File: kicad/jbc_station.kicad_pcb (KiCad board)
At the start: 2 copper layers, 275 parts, among them J1 PWR, J15 Conn_01x07, J2 Conn_01x02, J21 Conn_01x07, J3 Barcode, J4 Front panel, J5 Conn_01x03, J6 Conn_01x05, J7 Conn_01x04, J8 Conn_01x03, J9 Conn_01x07, Q1 BSS138, Q2 BSS138, Q3 BSS138, Q4 AON6448, Q5 AON6448, Q6 AON6448, Q7 AON6448, Q8 AON6448, Q9 AON6448, U1 L78L05_SOT89, U10 LM5106MM, U11 AD8221ARMZ, U12 LM5106MM, U13 AD8221ARMZ, U14 LM5106MM, U15 AD8221ARMZ, U2 LP2985-3.3, U3 ICL7660, U4 HT7463, U5 HT7463, U6 M24C64, U7 INA3221, U8 STM32F401CCUx, U9 CH9141K, Y1 Crystal, Y2 Crystal

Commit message: Route power stage
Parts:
- removed the C28 at (340.1, 97.6)
- removed the C43 at (264.4, -56.0)
- removed the C44 at (237.2, -52.9)
- removed D3: SMAJ5.0A, Diode_SMD_AKL:D_SMA
- removed the JP4 at (159.9, -47.1)
- removed the U10 at (237.9, -36.2)
- added C21: 2.2u, Capacitor_SMD:C_0805_2012Metric, F.Cu at (101.2, 106.0)
- added C22: 2.2u, Capacitor_SMD:C_0805_2012Metric, F.Cu at (97.7, 108.7)
- added C61: 22n, Capacitor_SMD:C_0805_2012Metric, F.Cu at (22.8, 77.1)
- added C62: 100n, Capacitor_SMD:C_0603_1608Metric_Pad1.08x0.95mm_HandSolder, F.Cu at (18.7, 79.4)
- added JP3: SolderJumper_2_Open, Jumper:SolderJumper-2_P1.3mm_Open_TrianglePad1.0x1.5mm, F.Cu at (105.8, 106.2)
- added JP5: SolderJumper_2_Open, Jumper:SolderJumper-2_P1.3mm_Open_TrianglePad1.0x1.5mm, F.Cu at (85.1, 15.3)
- added U12: AD8221ARMZ, Package_SO_AKL:MSOP-8_3x3mm_P0.65mm, F.Cu at (15.2, 76.3)
- added U6: XC6206PxxxMR, Package_TO_SOT_SMD:SOT-23-3, F.Cu at (97.7, 106.0)
- C3, C6, D11, D16, D19, D24, D27, D8, R32, R33, R40, R42, R58, R59, R66, R68, R84, R85, R92, R94: moved to B.Cu
- C45: value 10u -> 1u; footprint Capacitor_SMD:C_2220_5650Metric -> Capacitor_SMD:C_1206_3216Metric
- C46: value 10u -> 100u; footprint Capacitor_SMD:C_2220_5650Metric -> Capacitor_THT:C_Radial_D8.0mm_H11.5mm_P3.50mm
- C47: value 1u -> 10u; footprint Capacitor_SMD:C_1206_3216Metric -> Capacitor_SMD:C_2220_5650Metric
- C48: value 100n -> 10u; footprint Capacitor_SMD:C_0603_1608Metric_Pad1.08x0.95mm_HandSolder -> Capacitor_SMD:C_2220_5650Metric
- C49: value 47u -> 1u; footprint Capacitor_THT:C_Radial_D8.0mm_H11.5mm_P3.50mm -> Capacitor_SMD:C_1206_3216Metric
- C50: value 10u -> 100n; footprint Capacitor_SMD:C_2220_5650Metric -> Capacitor_SMD:C_0603_1608Metric_Pad1.08x0.95mm_HandSolder
- C51: value 10u -> 47u; footprint Capacitor_SMD:C_2220_5650Metric -> Capacitor_THT:C_Radial_D8.0mm_H11.5mm_P3.50mm
- C54: value 680pF -> 10u; footprint Capacitor_SMD:C_0805_2012Metric -> Capacitor_SMD:C_2220_5650Metric; moved to B.Cu
- C55: value 100n -> 10u; footprint Capacitor_SMD:C_0603_1608Metric_Pad1.08x0.95mm_HandSolder -> Capacitor_SMD:C_2220_5650Metric; moved to B.Cu
- C56: value 100n -> 680pF; footprint Capacitor_SMD:C_0603_1608Metric_Pad1.08x0.95mm_HandSolder -> Capacitor_SMD:C_0805_2012Metric
- C58: value 10n -> 100n; footprint Capacitor_SMD:C_0805_2012Metric -> Capacitor_SMD:C_0603_1608Metric_Pad1.08x0.95mm_HandSolder
- C59: value 22n -> 100n; footprint Capacitor_SMD:C_0805_2012Metric -> Capacitor_SMD:C_0603_1608Metric_Pad1.08x0.95mm_HandSolder
- C60: value 100n -> 10n; footprint Capacitor_SMD:C_0603_1608Metric_Pad1.08x0.95mm_HandSolder -> Capacitor_SMD:C_0805_2012Metric
- C72: renamed from C70; moved to B.Cu
- C73: renamed from C71; moved to B.Cu
- C90: renamed from C88; moved to B.Cu
- C91: renamed from C89; moved to B.Cu
- J7: footprint Connector_Molex:Molex_KK-254_AE-6410-04A_1x04_P2.54mm_Vertical -> Connector_PinHeader_2.54mm:PinHeader_1x04_P2.54mm_Vertical
- U11: value AD8221ARMZ -> LM5106MM; footprint Package_SO_AKL:MSOP-8_3x3mm_P0.65mm -> PCM_4ms_Package_SSOP:MSOP-10_3x3mm_P0.5mm
- moved R62 358.1 mm to (17.8, 111.3), turned to -90 degrees
- moved NT5 352.9 mm to (22.4, 114.3)
- moved D22 350.6 mm to (13.7, 112.0), turned to 180 degrees
- moved C78 349.0 mm to (13.7, 116.1), turned to 180 degrees
- moved R70 347.5 mm to (18.5, 118.1), turned to 90 degrees
- moved C75 346.7 mm to (12.7, 119.1), turned to -90 degrees
- moved R61 346.3 mm to (14.7, 119.2), turned to -90 degrees
- moved U14 346.0 mm to (22.8, 118.1)
- moved D30 344.7 mm to (13.1, 28.2), turned to 180 degrees
- moved R68 344.6 mm to (10.9, 94.2), turned to 90 degrees
- moved D19 342.0 mm to (13.5, 91.4)
- moved R59 341.7 mm to (13.0, 103.4), turned to -90 degrees
- moved D27 341.1 mm to (12.8, 7.62)
- moved C96 339.9 mm to (13.1, 32.3), turned to 180 degrees
- moved R94 338.5 mm to (10.3, 10.4), turned to 90 degrees
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- renumbered C21 to C23, C22 to C24, C23 to C25, C24 to C26, C25 to C27, C26 to C28, C27 to C29, C29 to C31, C30 to C32, C31 to C33, C32 to C34, C33 to C35, C34 to C36, C35 to C37, C36 to C38, C37 to C39, C38 to C40, C39 to C41, C40 to C42, C41 to C43, C42 to C44, C61 to C63, C62 to C64, C63 to C65, C64 to C66, C65 to C67, C66 to C68, C67 to C69, C68 to C70, C69 to C71, C72 to C74, C73 to C75, C74 to C76, C75 to C77, C76 to C78, C77 to C79, C78 to C80, C79 to C81, C80 to C82, C81 to C83, C82 to C84, C83 to C85, C84 to C86, C85 to C87, C86 to C88, C87 to C89, C90 to C92, C91 to C93, C92 to C94, C93 to C95, C94 to C96, C95 to C97, C96 to C98, JP3 to JP4, U9 to U10, U12 to U13, U13 to U14, U14 to U15, U15 to U16, U6 to U7, U7 to U8, U8 to U9
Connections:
- C42 pad 1: Net-(U9-X32MO) -> Net-(U10-X32MO)
- C45 pad 1: Net-(Q4-D) -> +12V
- C47 pad 1: Net-(D10-K) -> Net-(Q4-D)
- C47 pad 2: Net-(D7-K) -> GNDPWR
- C48 pad 1: Net-(D9-K) -> Net-(Q4-D)
- C48 pad 2: GNDA -> GNDPWR
- C49 pad 1: Net-(J9-Pin_3) -> Net-(D10-K)
- C49 pad 2: GNDPWR -> Net-(D7-K)
- C50 pad 1: Net-(J9-Pin_3) -> Net-(D9-K)
- C50 pad 2: GNDPWR -> GNDA
- C54 pad 1: Net-(D10-K) -> Net-(J9-Pin_3)
- C54 pad 2: Net-(C54-Pad2) -> GNDPWR
- C55 pad 1: /V_{OUT}1 -> Net-(J9-Pin_3)
- C55 pad 2: GNDA -> GNDPWR
- C56 pad 1: +5V -> Net-(D10-K)
- C56 pad 2: GNDA -> Net-(C56-Pad2)
- C57 pad 1: Net-(D13-K) -> /V_{OUT}1
- C58 pad 1: /int-out1/I_{SEN-} -> +5V
- C58 pad 2: Net-(U11-+) -> GNDA
- C59 pad 1: /TC_{OUT}1 -> Net-(D13-K)
- C60 pad 1: -5V -> /int-out1/I_{SEN-}
- C60 pad 2: GNDA -> Net-(U12-+)
- D14 pad 3: Net-(U11-+) -> Net-(U12-+)
- J3 pad 2: +3.3V -> /BARCODE_{TX}
- J3 pad 3: /BARCODE_{TX} -> /BARCODE_{RX}
- J3 pad 4: /BARCODE_{RX} -> Net-(J3-Pin_4)
- R20 pad 1: Net-(JP4-A) -> Net-(JP5-B)
- R34 pad 1: Net-(C54-Pad2) -> Net-(C56-Pad2)
- R37 pad 2: Net-(U10-RDT) -> Net-(U11-RDT)
- R47 pad 2: Net-(U11-+) -> Net-(U12-+)
- U10 pad 10: Net-(JP4-C) -> Net-(JP5-B)
- U10 pad 5: Net-(U9-X32MO) -> Net-(U10-X32MO)
- U11 pad 1: /int-out1/I_{SEN-} -> +12V
- U11 pad 2: Net-(R44-Pad2) -> Net-(D7-K)
- U11 pad 3: Net-(R44-Pad1) -> Net-(Q4-G)
- U11 pad 4: Net-(U11-+) -> Net-(D10-K)
- U11 pad 5: -5V -> (no net)
- U11 pad 6: GNDA -> Net-(U11-RDT)
- U11 pad 7: Net-(R45-Pad1) -> /PWM_{EN}
- U11 pad 8: +5V -> /PWM_{IN}1
- Y2 pad 2: Net-(U9-X32MO) -> GND
- Y2 pad 3: (no net) -> Net-(U10-X32MO)
- Y2 pad 4: (no net) -> GND
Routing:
- net GNDPWR: track 0.00 -> 613.1 mm, vias 0 -> 138
- net GNDA: track 0.00 -> 118.5 mm, vias 0 -> 57
- net +5V: track 0.00 -> 116.6 mm, vias 0 -> 3
- net -5V: track 0.00 -> 110.9 mm, vias 0 -> 3
- net Net-(J15-Pin_3): track 0.00 -> 94.7 mm, vias 0 -> 8
- net Net-(J21-Pin_3): track 0.00 -> 94.7 mm, vias 0 -> 8
- net Net-(J9-Pin_3): track 0.00 -> 94.7 mm, vias 0 -> 8
- net +3V3: track 0.00 -> 83.1 mm, vias 0 -> 3
- net Net-(D9-K): track 0.00 -> 69.9 mm, vias 0 -> 3
- net Net-(D25-K): track 0.00 -> 69.9 mm, vias 0 -> 3
- net Net-(D17-K): track 0.00 -> 69.9 mm, vias 0 -> 3
- net /V_{OUT}1: track 0.00 -> 69.5 mm, vias 0 -> 2
- net /V_{OUT}3: track 0.00 -> 69.5 mm, vias 0 -> 2
- net /V_{OUT}2: track 0.00 -> 69.5 mm, vias 0 -> 2
- net Net-(D13-K): track 0.00 -> 67.7 mm, vias 0 -> 1
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- added copper zone on F.Cu, net +48V
- added copper zone on F.Cu, net /int-out1/I_{SEN+}
- added copper zone on F.Cu, net /int-out1/I_{SEN-}
- added copper zone on F.Cu, net /int-out2/I_{SEN+}
- added copper zone on F.Cu, net /int-out2/I_{SEN-}
- added copper zone on F.Cu, net /int-out3/I_{SEN+}
- added copper zone on F.Cu, net /int-out3/I_{SEN-}
- added copper zone on B.Cu, net GND
- added copper zone on F.Cu, net GND
- added copper zone on B.Cu, net GNDA
- added copper zone on F.Cu, net GNDA
- added copper zone on B.Cu, net GNDPWR
- added copper zone on F.Cu, net GNDPWR
- added copper zone on F.Cu, net Net-(D10-K)
- added copper zone on F.Cu, net Net-(D18-K)
- added copper zone on F.Cu, net Net-(D26-K)
- added copper zone on B.Cu, net Net-(J15-Pin_3)
- added copper zone on F.Cu, net Net-(J15-Pin_3)
- added copper zone on B.Cu, net Net-(J21-Pin_3)
- added copper zone on F.Cu, net Net-(J21-Pin_3)
- added copper zone on B.Cu, net Net-(J9-Pin_3)
- added copper zone on F.Cu, net Net-(J9-Pin_3)
- added copper zone on F.Cu, net Net-(Q4-D)
- added copper zone on F.Cu, net Net-(Q6-D)
- added copper zone on F.Cu, net Net-(Q8-D)
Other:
- board outline added: 125 x 125 mm

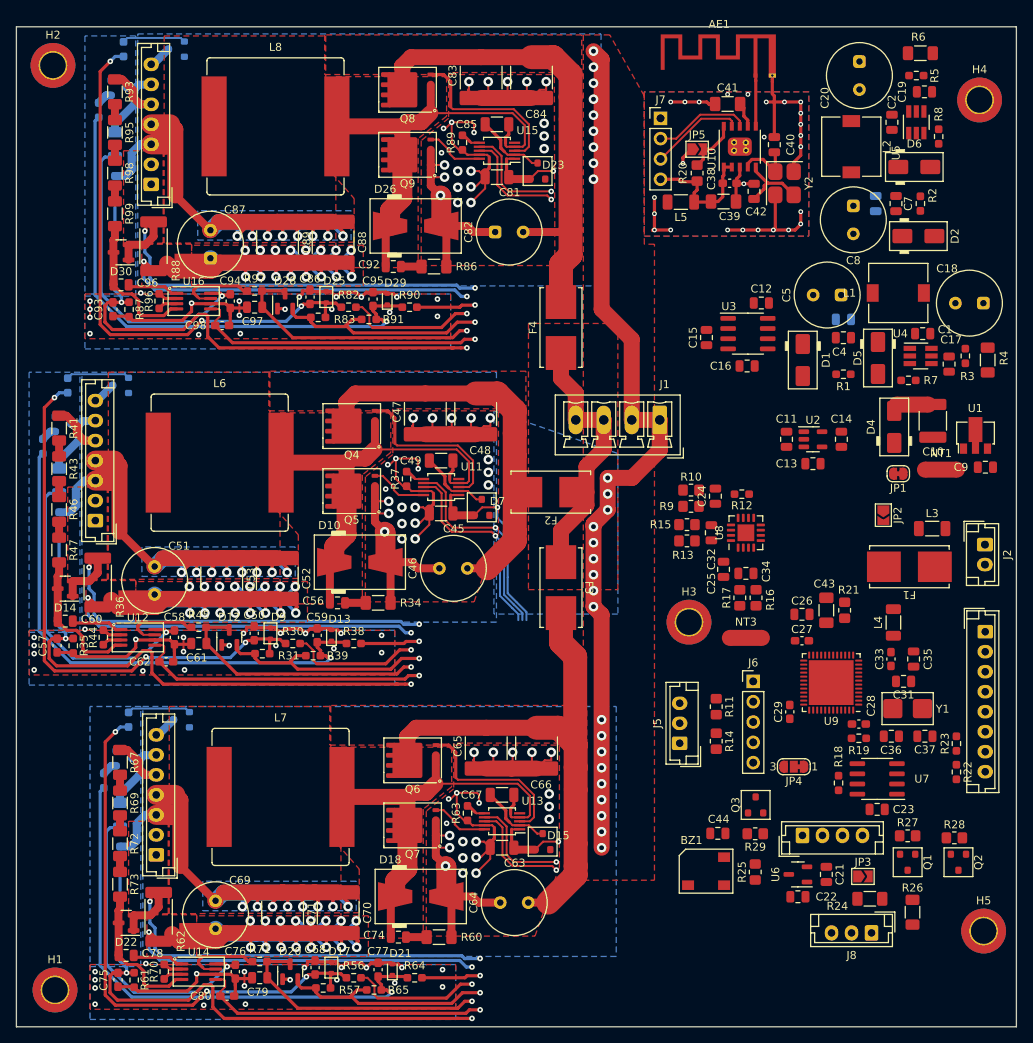
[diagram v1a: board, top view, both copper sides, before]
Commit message: Route DC-DCs, BT
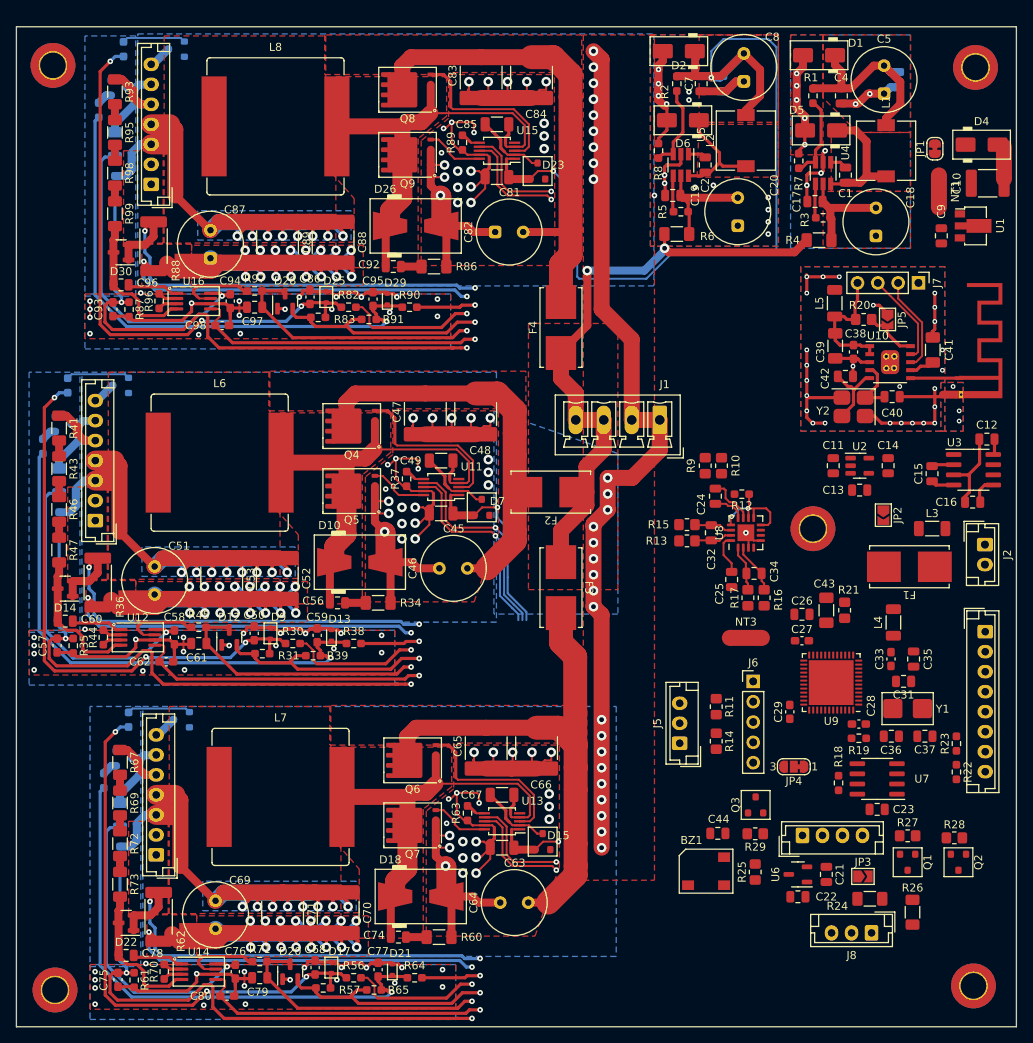
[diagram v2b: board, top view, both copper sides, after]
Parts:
- moved AE1 45.7 mm to (118.1, 43.9), turned to -90 degrees
- moved JP1 40.9 mm to (114.8, 15.2), turned to 90 degrees
- moved C41 40.0 mm to (114.5, 40.4), turned to -90 degrees
- moved J7 38.2 mm to (112.8, 32.0), turned to -90 degrees
- moved D1 38.2 mm to (100.3, 3.56), turned to 180 degrees
- moved R6 37.9 mm to (82.5, 25.9), turned to 0 degrees
- moved D2 37.8 mm to (82.8, 3.05), turned to 180 degrees
- moved D4 36.9 mm to (120.7, 14.7), turned to 0 degrees
- moved R8 35.1 mm to (80.3, 15.5), turned to 90 degrees
- moved R1 35.0 mm to (99.6, 8.64), turned to -90 degrees
- moved NT1 34.8 mm to (115.3, 20.6), turned to 90 degrees
- moved C40 34.8 mm to (109.5, 46.2), turned to 0 degrees
- moved C19 34.0 mm to (82.0, 21.1), turned to 180 degrees
- moved R5 34.0 mm to (83.1, 23.1), turned to 0 degrees
- moved R2 33.9 mm to (82.5, 7.11), turned to -90 degrees
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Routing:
- net +12V: track 44.6 -> 152.5 mm, vias 3 -> 4
- net GNDPWR: track 613.1 -> 672.1 mm, vias 138 -> 163
- net +48V: track 32.6 -> 75.7 mm, vias 0 -> 2
- net +5VL: track 0.00 -> 25.7 mm
- net Net-(D5-K): track 0.00 -> 15.9 mm
- net Net-(#FLG03-pwr): track 0.00 -> 15.1 mm
- net GND: track 58.2 -> 73.0 mm, vias 26 -> 30
- net Net-(D6-K): track 0.00 -> 14.4 mm
- net Net-(U8-CRITICAL): track 0.00 -> 13.4 mm, vias 0 -> 2
- net Net-(#FLG04-pwr): track 0.00 -> 13.3 mm
- net Net-(U5-FB): track 0.00 -> 10.8 mm
- net Net-(U4-FB): track 0.00 -> 10.6 mm
- net Net-(U8-IN+3): track 0.00 -> 6.35 mm
- net Net-(U8-IN-1): track 0.00 -> 6.30 mm
- net Net-(U8-IN-3): track 0.00 -> 5.77 mm
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- added copper zone on F.Cu, net +12V
- added copper zone on F.Cu, net +5VL
- added copper zone on F.Cu, net Net-(#FLG04-pwr)
- added copper zone on F.Cu, net Net-(D5-K)
- added copper zone on F.Cu, net Net-(D6-K)

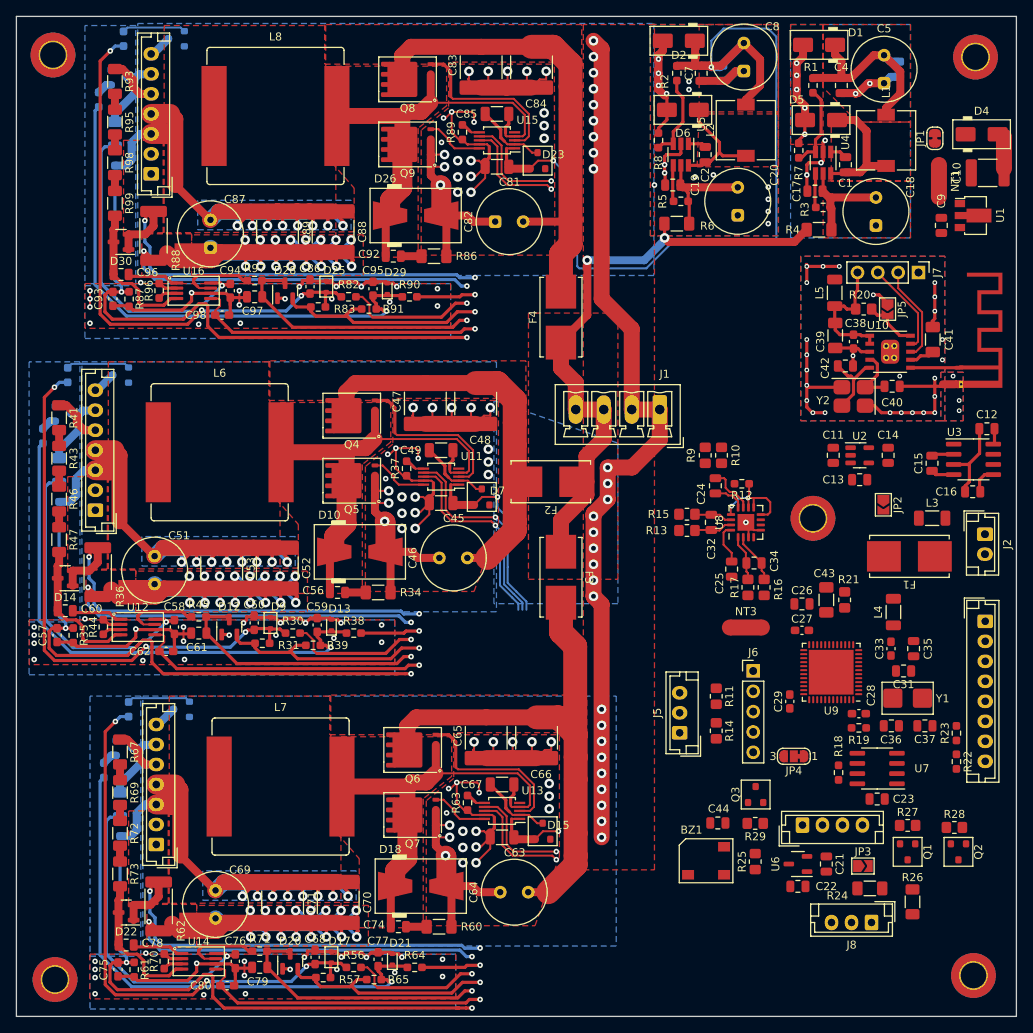
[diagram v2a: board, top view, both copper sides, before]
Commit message: Route LDOs
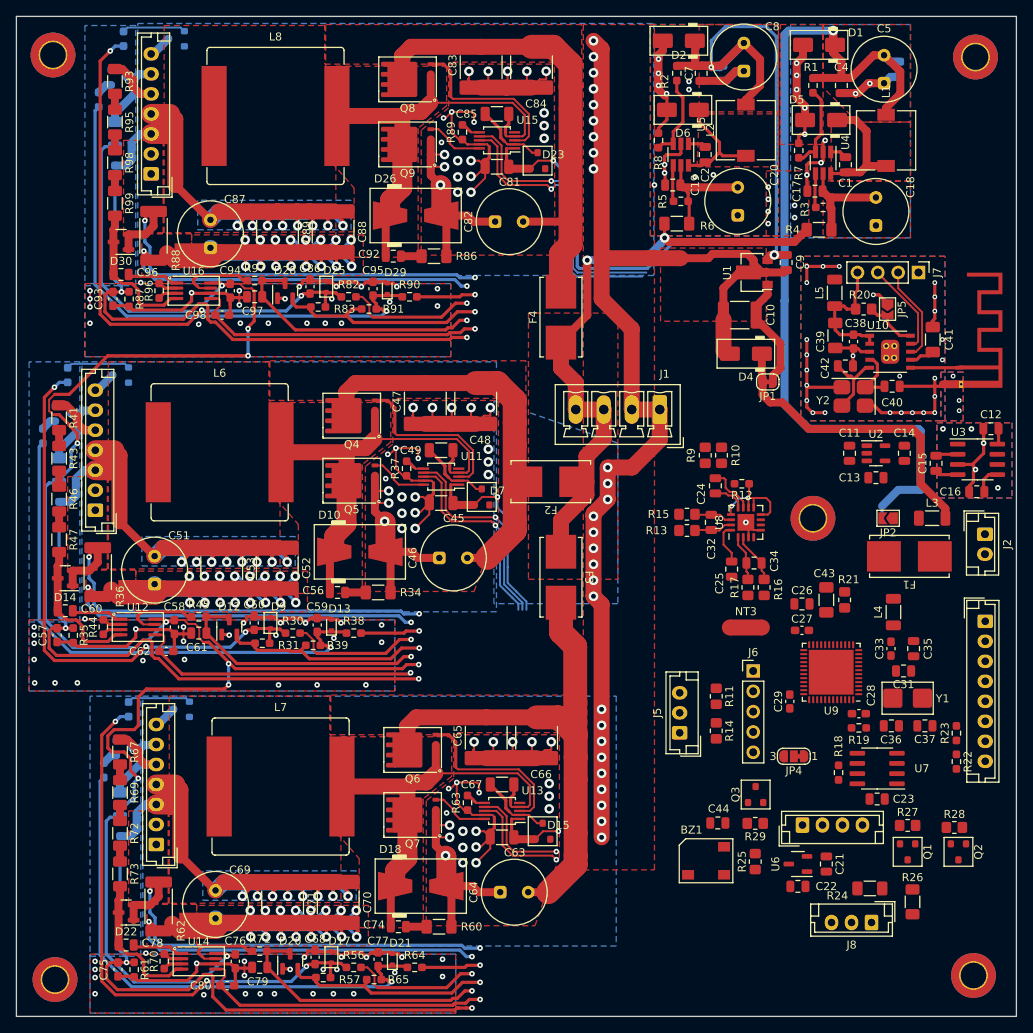
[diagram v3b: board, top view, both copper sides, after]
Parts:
- removed JP3: SolderJumper_2_Open, Jumper:SolderJumper-2_P1.3mm_Open_TrianglePad1.0x1.5mm
- moved NT2 41.8 mm to (88.4, 39.9), turned to -90 degrees
- moved D4 40.3 mm to (91.2, 42.2), turned to 180 degrees
- moved JP1 36.9 mm to (93.9, 45.7), turned to 180 degrees
- moved C10 35.7 mm to (90.4, 37.3), turned to 180 degrees
- moved NT1 35.6 mm to (81.0, 30.2), turned to 0 degrees
- moved U1 28.8 mm to (91.9, 32.0), turned to 180 degrees
- moved C9 19.9 mm to (96.2, 30.8), turned to 90 degrees
- moved C14 2.05 mm to (111.0, 54.6)
- moved C11 2.05 mm to (104.1, 54.6)
- moved C13 2.05 mm to (107.4, 57.7)
- moved U2 2.05 mm to (107.4, 54.6)
- moved JP2 1.79 mm to (109.0, 62.7), turned to 180 degrees
- moved C15 0.51 mm to (115.0, 55.9)
- moved C12 0.51 mm to (121.8, 51.5)
- moved C16 0.51 mm to (120.0, 59.4)
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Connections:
- C22 pad 1: +5V -> +5VL
- U6 pad 3: +5V -> +5VL
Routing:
- net +5V: track 118.6 -> 256.2 mm, vias 3 -> 10
- net +5VL: track 25.7 -> 114.9 mm, vias 0 -> 1
- net /+5VSB: track 0.00 -> 38.7 mm
- net Net-(#FLG07-pwr): track 0.00 -> 24.4 mm
- net /PWM_{EN}: track 53.1 -> 75.5 mm
- net /PWM_{IN}3: track 13.6 -> 35.7 mm
- net GNDPWR: track 672.1 -> 679.0 mm, vias 163 -> 165
- net +12V: track 152.5 -> 158.0 mm, vias 4 -> 5
- net +3V3: track 83.1 -> 81.5 mm
- net /V_{OUT}2: track 69.5 -> 70.2 mm
- net GND: track 73.0 -> 73.3 mm, vias 30 -> 35
- net GNDA: track 118.5 -> 118.7 mm, vias 57 -> 73
- added copper zone on F.Cu, net Net-(#FLG07-pwr)

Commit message: Route finish
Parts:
- removed L5: 1u, Inductor_SMD:L_1206_3216Metric_Pad1.22x1.90mm_HandSolder
- removed NT2, NT3: NetTie_2, NetTie:NetTie-2_SMD_Pad2.0mm
- added C30: 2.2u, Capacitor_SMD:C_0805_2012Metric, F.Cu at (101.3, 29.2)
- added C99: 2.2u, Capacitor_SMD:C_0805_2012Metric, F.Cu at (101.3, 34.8)
- added U17: XC6206PxxxMR, Package_TO_SOT_SMD:SOT-23-3, F.Cu at (101.3, 32.0)
- moved C11 22.6 mm to (118.4, 72.2), turned to 180 degrees
- moved C15 18.8 mm to (104.5, 71.5)
- moved C16 18.8 mm to (109.6, 75.0)
- moved C12 18.8 mm to (111.4, 67.2)
- moved U3 18.8 mm to (109.7, 71.0)
- moved U2 18.0 mm to (118.4, 68.9), turned to 90 degrees
- moved C13 17.9 mm to (121.4, 68.9), turned to 90 degrees
- moved BZ1 13.2 mm to (88.1, 118.6), turned to 90 degrees
- moved C14 13.0 mm to (118.4, 65.3), turned to 180 degrees
- moved C44 11.7 mm to (88.0, 112.5), turned to 180 degrees
- moved R25 10.8 mm to (93.7, 116.3), turned to 0 degrees
- moved L4 9.11 mm to (109.7, 83.6), turned to 180 degrees
- moved C25 9.04 mm to (95.0, 76.2)
- moved F1 8.57 mm to (111.6, 58.9)
- moved J2 8.57 mm to (121.1, 56.2)
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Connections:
- C10 pad 2: Net-(#FLG07-pwr) -> GND
- C12 pad 2: +5V -> /+5VSB
- C50 pad 2: GNDA -> GND
- C57 pad 2: GNDA -> GND
- C58 pad 2: GNDA -> GND
- C59 pad 2: GNDA -> GND
- C61 pad 2: GNDA -> GND
- C62 pad 2: GNDA -> GND
- C68 pad 2: GNDA -> GND
- C75 pad 2: GNDA -> GND
- C76 pad 2: GNDA -> GND
- C77 pad 2: GNDA -> GND
- C79 pad 2: GNDA -> GND
- C80 pad 2: GNDA -> GND
- C86 pad 2: GNDA -> GND
- C9 pad 1: Net-(#FLG07-pwr) -> GND
- C93 pad 2: GNDA -> GND
- C94 pad 2: GNDA -> GND
- C95 pad 2: GNDA -> GND
- C97 pad 2: GNDA -> GND
- C98 pad 2: GNDA -> GND
- D12 pad 1: GNDA -> GND
- D12 pad 2: +3V3 -> +3.3V
- D13 pad 2: GNDA -> GND
- D17 pad 2: GNDA -> GND
- D20 pad 1: GNDA -> GND
- D20 pad 2: +3V3 -> +3.3V
- D21 pad 2: GNDA -> GND
- D25 pad 2: GNDA -> GND
- D28 pad 1: GNDA -> GND
- D28 pad 2: +3V3 -> +3.3V
- D29 pad 2: GNDA -> GND
- D9 pad 2: GNDA -> GND
- H3 pad 1: unconnected-(H3-Pad1) -> GND
- H5 pad 1: unconnected-(H5-Pad1) -> GND
- J2 pad 1: GNDPWR -> GND
- J6 pad 1: +3V3 -> +3.3V
- NT1 pad 2: Net-(#FLG07-pwr) -> GND
- R10 pad 1: /int-out1/I_{SEN-} -> /int-out3/I_{SEN-}
- R13 pad 1: /int-out2/I_{SEN+} -> /int-out1/I_{SEN+}
- R15 pad 1: /int-out2/I_{SEN-} -> /int-out1/I_{SEN-}
- R16 pad 1: /int-out3/I_{SEN+} -> /int-out2/I_{SEN+}
- R17 pad 1: /int-out3/I_{SEN-} -> /int-out2/I_{SEN-}
- R25 pad 2: +5V -> +5VL
- R31 pad 1: +3V3 -> +3.3V
- R35 pad 2: GNDA -> GND
- R39 pad 1: +3V3 -> +3.3V
- R57 pad 1: +3V3 -> +3.3V
- R61 pad 2: GNDA -> GND
- R65 pad 1: +3V3 -> +3.3V
- R83 pad 1: +3V3 -> +3.3V
- R87 pad 2: GNDA -> GND
- R9 pad 1: /int-out1/I_{SEN+} -> /int-out3/I_{SEN+}
- R91 pad 1: +3V3 -> +3.3V
- U1 pad 2: Net-(#FLG07-pwr) -> GND
- U12 pad 6: GNDA -> GND
- U14 pad 6: GNDA -> GND
- U16 pad 6: GNDA -> GND
- U3 pad 8: +5V -> /+5VSB
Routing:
- net GND: track 73.3 -> 515.9 mm, vias 35 -> 347
- net +3.3V: track 5.15 -> 414.1 mm, vias 0 -> 10
- net -5V: track 114.0 -> 322.7 mm, vias 3 -> 9
- net /PWM_{EN}: track 75.5 -> 259.4 mm, vias 3 -> 13
- net /V_{OUT}2: track 70.2 -> 200.9 mm, vias 2 -> 4
- net +12V: track 158.0 -> 284.2 mm, vias 5 -> 8
- net /TC_{OUT}2: track 32.9 -> 158.5 mm, vias 1 -> 3
- net GNDA: track 118.7 -> 0.00 mm, vias 73 -> 0
- net /V_{OUT}3: track 69.2 -> 168.9 mm, vias 2 -> 3
- net +5VL: track 114.9 -> 214.0 mm, vias 1 -> 4
- net /TC_{OUT}3: track 32.9 -> 131.7 mm, vias 1 -> 2
- net /BT_{TX}: track 12.1 -> 110.5 mm, vias 0 -> 3
- net /SLEEP_{SEN}3: track 7.38 -> 105.0 mm, vias 1 -> 4
- net /HNDL_{SEN}3: track 16.4 -> 112.3 mm, vias 1 -> 4
- net /HNDL_{SEN}1: track 16.4 -> 109.7 mm, vias 1 -> 4
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- removed copper zone on B.Cu, net GNDA
- removed copper zone on F.Cu, net GNDA
- removed copper zone on F.Cu, net Net-(#FLG07-pwr)
- removed copper zone on F.Cu, net Net-(U4-VIN)
